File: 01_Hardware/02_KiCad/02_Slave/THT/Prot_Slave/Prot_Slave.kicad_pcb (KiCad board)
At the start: 2 copper layers, 14 parts, among them J10 Conn_01x22_Female, J20 Conn_01x22_Female, J5 Screw_Terminal_01x04, J6 Screw_Terminal_01x04, U1 LM393P, U2 AO3400A, U3 AO3400A

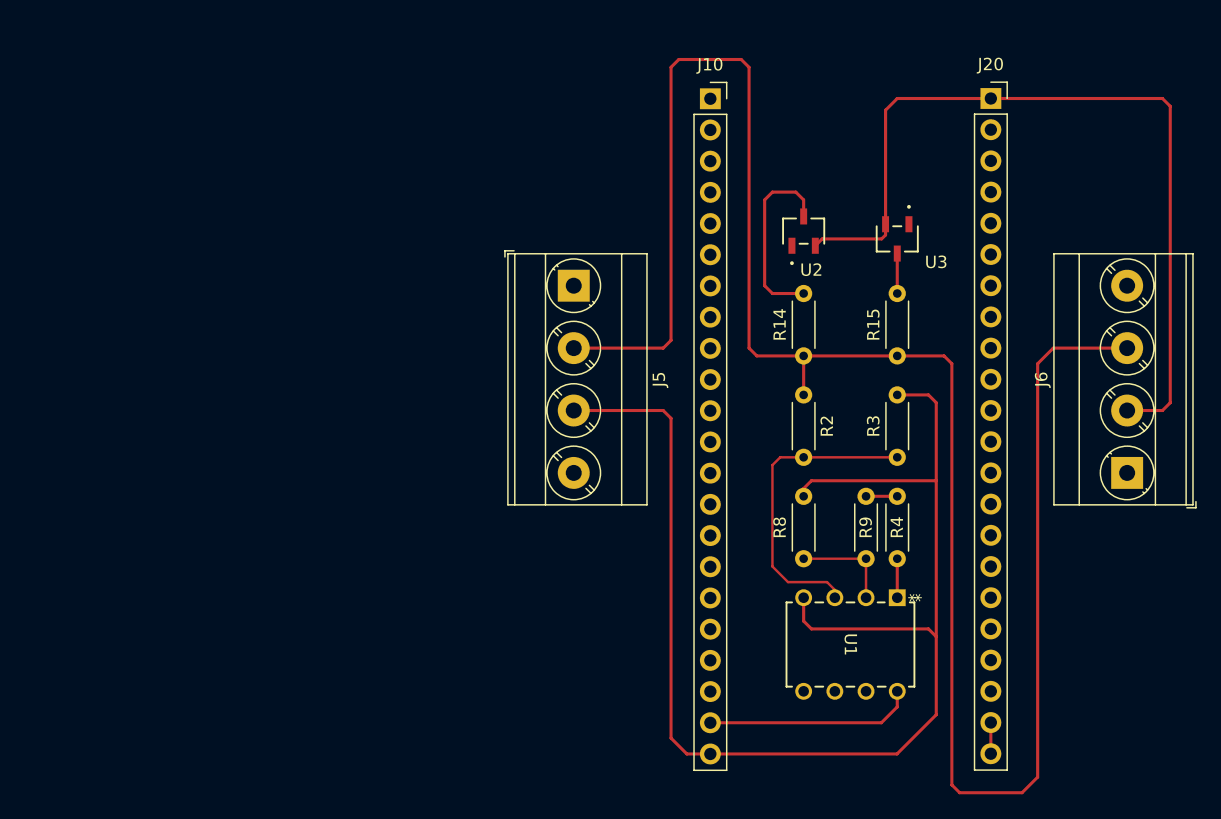
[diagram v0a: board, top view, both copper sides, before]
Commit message: Master and Slave Prototyp finsished! JLCPCB ordered
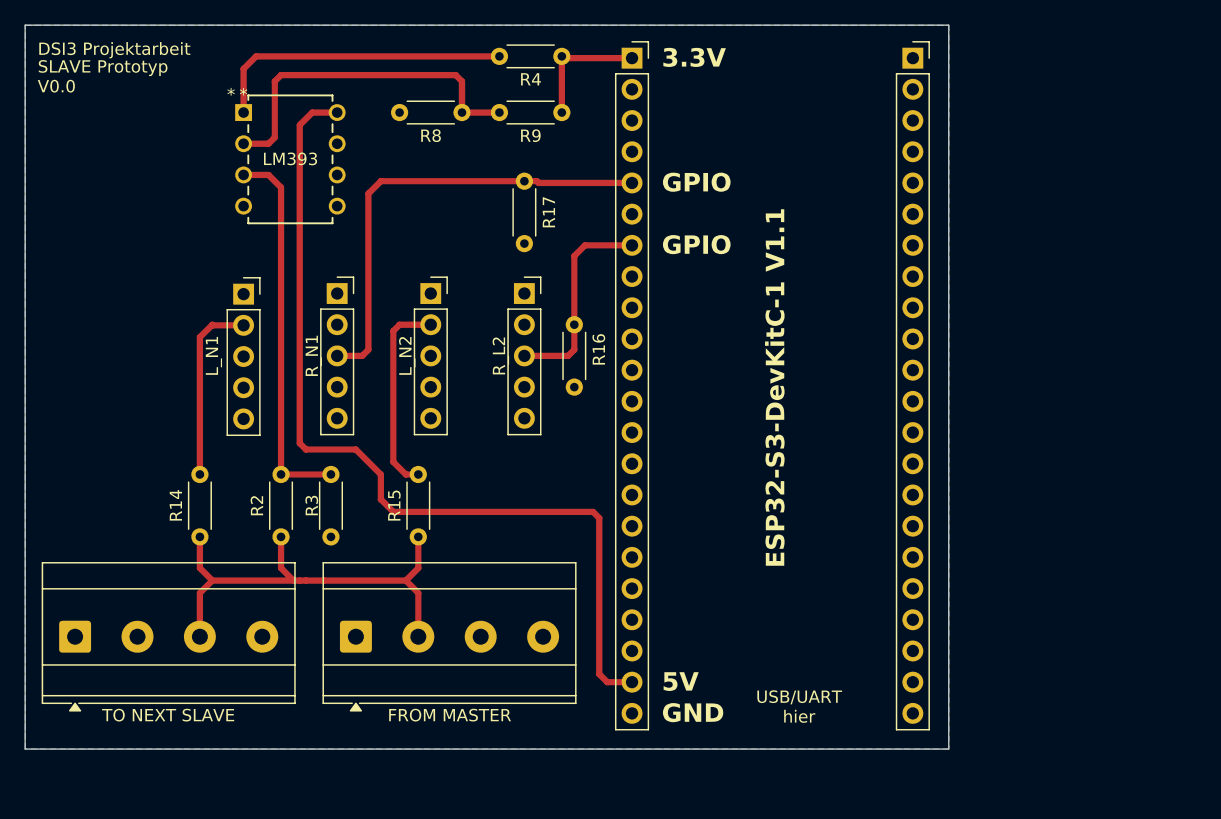
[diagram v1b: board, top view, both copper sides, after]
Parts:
- removed U2, U3: AO3400A, AO3400A:SOT-23-3L_AOS
- added L_N1: NMOS1, Connector_PinSocket_2.54mm:PinSocket_1x05_P2.54mm_Vertical, F.Cu at (124.0, 104.2)
- added L_N2: NMOS1, Connector_PinSocket_2.54mm:PinSocket_1x05_P2.54mm_Vertical, F.Cu at (139.2, 104.1)
- added R16: 10k, Resistor_THT:R_Axial_DIN0204_L3.6mm_D1.6mm_P5.08mm_Horizontal, F.Cu at (150.9, 111.8)
- added R17: 10k, Resistor_THT:R_Axial_DIN0204_L3.6mm_D1.6mm_P5.08mm_Horizontal, F.Cu at (146.8, 100.1)
- added R_L2: NMOS2, Connector_PinSocket_2.54mm:PinSocket_1x05_P2.54mm_Vertical, F.Cu at (146.8, 104.1)
- added R_N1: NMOS1, Connector_PinSocket_2.54mm:PinSocket_1x05_P2.54mm_Vertical, F.Cu at (131.6, 104.1)
- J5: value Screw_Terminal_01x04 -> FROM MASTER
- J6: value Screw_Terminal_01x04 -> TO NEXT SLAVE
- U1: value LM393P -> LM393
- moved J6 86.7 mm to (110.2, 132.1), turned to 0 degrees
- moved U1 66.3 mm to (124.0, 89.4), turned to 0 degrees
- moved R4 52.2 mm to (144.8, 84.8), turned to 0 degrees
- moved R14 51.3 mm to (120.4, 124.0)
- moved R3 46.1 mm to (131.1, 118.9), turned to -90 degrees
- moved R8 45.7 mm to (141.7, 89.4), turned to 180 degrees
- moved R2 44.1 mm to (127.0, 124.0), turned to 90 degrees
- moved R15 41.7 mm to (138.2, 124.0)
- moved R9 39.9 mm to (149.9, 89.4), turned to 180 degrees
- moved J5 33.6 mm to (133.1, 132.1), turned to 0 degrees
- moved J10 7.18 mm to (155.6, 85.0)
- moved J20 7.15 mm to (178.4, 85.0)
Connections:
- J10 pad 11: Net-(U2-Pad1) -> unconnected-(J10-Pin_11-Pad11)
- J10 pad 12: Net-(U3-Pad1) -> unconnected-(J10-Pin_12-Pad12)
- J10 pad 5: unconnected-(J10-Pad5) -> Gate_N1
- J10 pad 7: unconnected-(J10-Pad7) -> Gate_N2
- J20 pad 1: GND -> unconnected-(J20-Pin_1-Pad1)
- J20 pad 21: GND -> unconnected-(J20-Pin_21-Pad21)
- J20 pad 22: GND -> unconnected-(J20-Pin_22-Pad22)
- R14 pad 2: Net-(R14-Pad2) -> Drain_N1
- R15 pad 2: Net-(R15-Pad2) -> Drain_N2
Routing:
- net GND: track 181.9 -> 0.00 mm
- net Bus: track 163.9 -> 37.7 mm
- net 5V: track 17.0 -> 73.1 mm
- net Gate_N1: track 0.00 -> 37.6 mm
- net LM393_Out: track 3.17 -> 24.8 mm
- net LM393_IN-: track 8.26 -> 28.6 mm
- net Gate_N2: track 0.00 -> 17.0 mm
- net Drain_N2: track 0.00 -> 16.4 mm
- net Net-(R14-Pad2): track 15.5 -> 0.00 mm
- net Drain_N1: track 0.00 -> 15.2 mm
- net 3.3V: track 2.54 -> 10.3 mm
- net LM393_IN+: track 25.2 -> 30.9 mm
- net Net-(R15-Pad2): track 3.25 -> 0.00 mm
- added copper zone on B.Cu, net GND
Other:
- board outline added: 75.2 x 58.9 mm
- board text added: "3.3V"
- board text added: "5V"
- board text added: "DSI3 Projektarbeit"
- board text added: "ESP32-S3-DevKitC-1 V1.1"
- board text added: "GND"
- board text added: "GPIO"
- board text added: "SLAVE Prototyp V0.0"
- board text added: "USB/UART hier"
